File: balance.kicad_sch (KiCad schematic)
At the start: 5 parts, among them Q1 AO3400A

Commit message: schematic: Assign some footprints
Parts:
- D1: footprint (none) -> LED_SMD:LED_0603_1608Metric
- R20, R22: footprint (none) -> Resistor_SMD:R_0603_1608Metric
- R21: footprint (none) -> Resistor_SMD:R_2512_6332Metric; Part Number (none) -> RPL-12K10R0FT
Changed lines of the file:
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@@
 			)
 		)
-		(property "Footprint" ""
+		(property "Footprint" "Resistor_SMD:R_0603_1608Metric"
 			(at 120.65 62.23 0)
 			(effects
@@
 			)
 		)
-		(property "Footprint" ""
+		(property "Footprint" "Resistor_SMD:R_0603_1608Metric"
 			(at 137.16 45.72 0)
 			(effects
@@
 			)
 		)
-		(property "Footprint" ""
+		(property "Footprint" "Resistor_SMD:R_2512_6332Metric"
 			(at 130.302 50.8 90)
 			(effects
@@
 		)
 		(property "Description" "Resistor"
+			(at 132.08 50.8 0)
+			(effects
+				(font
+					(size 1.27 1.27)
+				)
+				(hide yes)
+			)
+		)
+		(property "Part Number" " RPL-12K10R0FT"
 			(at 132.08 50.8 0)
 			(effects
@@
 			)
 		)
-		(property "Footprint" ""
+		(property "Footprint" "LED_SMD:LED_0603_1608Metric"
 			(at 137.16 52.07 90)
 			(effects

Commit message: schematic: Add BOM role
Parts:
- D1: Role (none) -> Balance active LED
- Q1: Role (none) -> Balance MOSFET
- R20: Role (none) -> Balance MOSFET gate resistor
- R21: Role (none) -> Balance resistor
- R22: Role (none) -> Balance active LED resistor
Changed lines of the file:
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@@
+			)
+		)
+		(property "Role" "Balance MOSFET gate resistor"
+			(at 120.65 62.23 0)
+			(effects
+				(font
+					(size 1.27 1.27)
+				)
+				(hide yes)
 			)
 		)
@@
 			)
 		)
+		(property "Role" "Balance active LED resistor"
+			(at 137.16 45.72 0)
+			(effects
+				(font
+					(size 1.27 1.27)
+				)
+				(hide yes)
+			)
+		)
 		(pin "1"
 		)
@@
 			)
 		)
+		(property "Role" "Balance resistor"
+			(at 132.08 50.8 0)
+			(effects
+				(font
+					(size 1.27 1.27)
+				)
+				(hide yes)
+			)
+		)
 		(pin "1"
 		)
@@
 			)
 		)
+		(property "Role" "Balance active LED"
+			(at 137.16 52.07 0)
+			(effects
+				(font
+					(size 1.27 1.27)
+				)
+				(hide yes)
+			)
+		)
 		(pin "2"
 		)
@@
 			(at 129.54 62.23 0)
 			(effects
+				(font
+					(size 1.27 1.27)
+				)
+				(hide yes)
+			)
+		)
+		(property "Role" "Balance MOSFET"
+			(at 129.54 62.23 0)
+			(effects

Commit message: schematic: Assign some more real components to passives
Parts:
- R20: Part Number (none) -> 0603WAF3001T5E
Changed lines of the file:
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@@
+			)
+		)
+		(property "Part Number" "0603WAF3001T5E"
+			(at 120.65 62.23 0)
+			(effects
+				(font
+					(size 1.27 1.27)
+				)
+				(hide yes)
 			)
 		)

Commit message: schematic: Cleanup
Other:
- company: (none) -> York Formula Student
- title: (none) -> Battery Management System
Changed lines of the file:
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@@
 	(generator_version "8.0")
 	(paper "A4")
+	(title_block
+		(title "Battery Management System")
+		(date "2025-02-08")
+		(rev "1")
+		(company "York Formula Student")
+	)
 	(junction
 		(at 132.08 55.88)

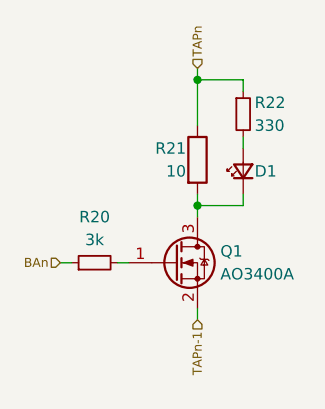
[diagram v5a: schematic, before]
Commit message: schematic: Re-annotate designators
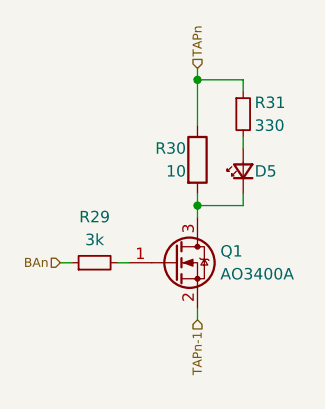
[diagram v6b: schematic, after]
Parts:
- renumbered D1 to D5, R20 to R29, R21 to R30, R22 to R31

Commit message: schematic: Cleanup BOM
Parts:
- D5: Dist (none) -> LCSC; Dist # (none) -> C84263; Mfr (none) -> Foshan NationStar Optoelectronics; Mfr # (none) -> NCD0603R1; Role Balance active LED -> (none)
- Q1: Dist (none) -> LCSC; Dist # (none) -> C347475; Mfr (none) -> UMW; Mfr # (none) -> AO3400A; Role Balance MOSFET -> (none)
- R29: Dist (none) -> LCSC; Dist # (none) -> C4211; Mfr (none) -> Uni-Royal; Mfr # (none) -> 0603WAF3001T5E; Part Number 0603WAF3001T5E -> (none); Role Balance MOSFET gate resistor -> (none)
- R30: Dist (none) -> LCSC; Dist # (none) -> C2991665; Mfr (none) -> FH; Mfr # (none) -> RPL-12K10R0FT; Part Number RPL-12K10R0FT -> (none); Role Balance resistor -> (none)
- R31: Dist (none) -> LCSC; Dist # (none) -> C23138; Mfr (none) -> Uni-Royal; Mfr # (none) -> 0603WAF3300T5E; Role Balance active LED resistor -> (none)
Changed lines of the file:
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@@
 			)
 		)
-		(property "Role" "Balance MOSFET gate resistor"
+		(property "Dist #" "C4211"
 			(at 120.65 62.23 0)
 			(effects
@@
 			)
 		)
-		(property "Part Number" "0603WAF3001T5E"
+		(property "Mfr" "Uni-Royal"
+			(at 120.65 62.23 0)
+			(effects
+				(font
+					(size 1.27 1.27)
+				)
+				(hide yes)
+			)
+		)
+		(property "Mfr #" "0603WAF3001T5E"
+			(at 120.65 62.23 0)
+			(effects
+				(font
+					(size 1.27 1.27)
+				)
+				(hide yes)
+			)
+		)
+		(property "Dist" "LCSC"
 			(at 120.65 62.23 0)
 			(effects
@@
 			)
 		)
-		(property "Role" "Balance active LED resistor"
+		(property "Dist #" "C23138"
+			(at 137.16 45.72 0)
+			(effects
+				(font
+					(size 1.27 1.27)
+				)
+				(hide yes)
+			)
+		)
+		(property "Mfr" "Uni-Royal"
+			(at 137.16 45.72 0)
+			(effects
+				(font
+					(size 1.27 1.27)
+				)
+				(hide yes)
+			)
+		)
+		(property "Mfr #" "0603WAF3300T5E"
+			(at 137.16 45.72 0)
+			(effects
+				(font
+					(size 1.27 1.27)
+				)
+				(hide yes)
+			)
+		)
+		(property "Dist" "LCSC"
 			(at 137.16 45.72 0)
 			(effects
@@
 			)
 		)
-		(property "Part Number" " RPL-12K10R0FT"
+		(property "Dist #" "C2991665"
 			(at 132.08 50.8 0)
 			(effects
@@
 			)
 		)
-		(property "Role" "Balance resistor"
+		(property "Mfr" "FH"
+			(at 132.08 50.8 0)
+			(effects
+				(font
+					(size 1.27 1.27)
+				)
+				(hide yes)
+			)
+		)
+		(property "Mfr #" "RPL-12K10R0FT"
+			(at 132.08 50.8 0)
+			(effects
+				(font
+					(size 1.27 1.27)
+				)
+				(hide yes)
+			)
+		)
+		(property "Dist" "LCSC"
 			(at 132.08 50.8 0)
 			(effects
@@
 			)
 		)
-		(property "Role" "Balance active LED"
+		(property "Dist #" "C84263"
+			(at 137.16 52.07 0)
+			(effects
+				(font
+					(size 1.27 1.27)
+				)
+				(hide yes)
+			)
+		)
+		(property "Mfr" "Foshan NationStar Optoelectronics"
+			(at 137.16 52.07 0)
+			(effects
+				(font
+					(size 1.27 1.27)
+				)
+				(hide yes)
+			)
+		)
+		(property "Mfr #" "NCD0603R1"
+			(at 137.16 52.07 0)
+			(effects
+				(font
+					(size 1.27 1.27)
+				)
+				(hide yes)
+			)
+		)
+		(property "Dist" "LCSC"
 			(at 137.16 52.07 0)
 			(effects
@@
 			)
 		)
-		(property "Role" "Balance MOSFET"
+		(property "Dist #" "C347475"
 			(at 129.54 62.23 0)
 			(effects
+				(font
+					(size 1.27 1.27)
+				)
+				(hide yes)
+			)
+		)
+		(property "Mfr" "UMW"
+			(at 129.54 62.23 0)
+			(effects
+				(font
+					(size 1.27 1.27)
+				)
+				(hide yes)
+			)
+		)
+		(property "Mfr #" "AO3400A"
+			(at 129.54 62.23 0)
+			(effects
+				(font
+					(size 1.27 1.27)
+				)
+				(hide yes)
+			)
+		)
+		(property "Dist" "LCSC"
+			(at 129.54 62.23 0)
+			(effects
